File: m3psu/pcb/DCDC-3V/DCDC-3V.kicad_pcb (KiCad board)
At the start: 2 copper layers, 39.5 x 39.5 mm, 69 parts, among them IC1 LTC2975, IC2 TPS62132, IC3 LTC2975, J1 WEST TOP, J2 WEST BOT, J3 NORTH TOP, J4 EAST TOP, J5 EAST BOT, J6 NORTH BOT, Q1 NFET_GDS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

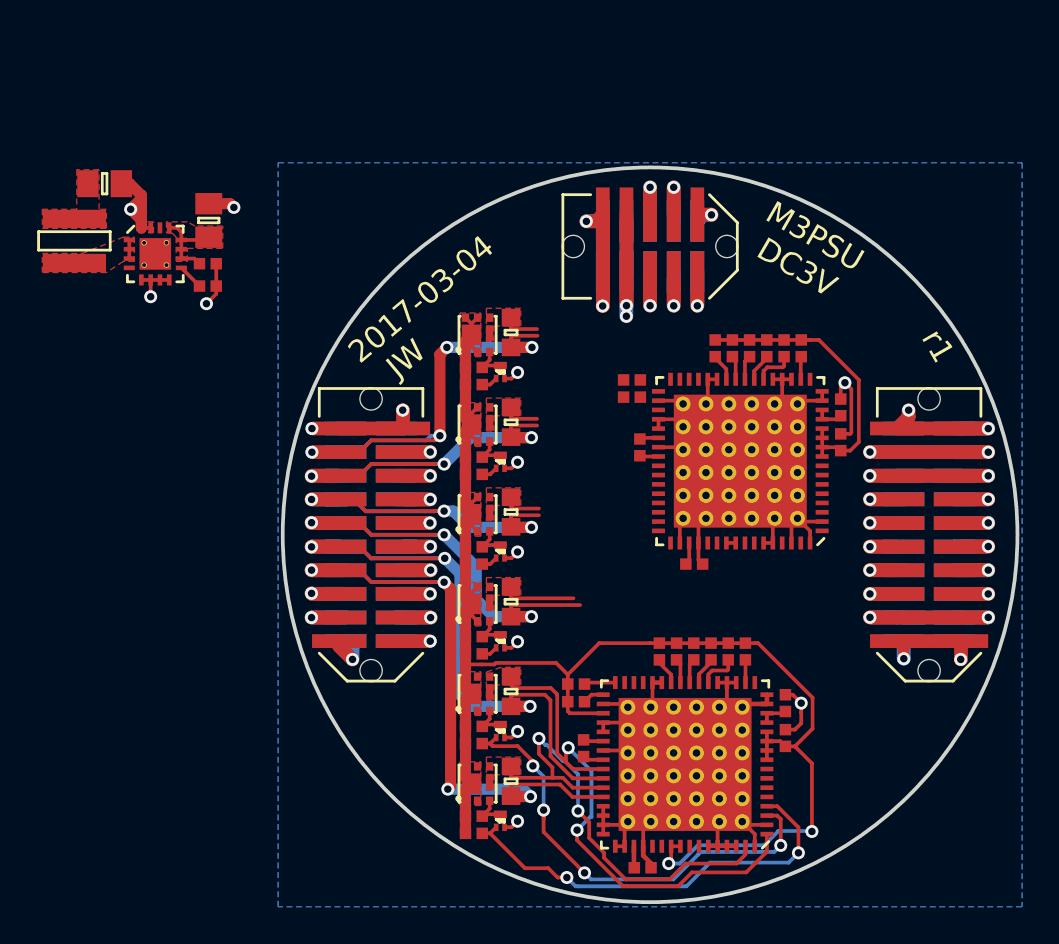
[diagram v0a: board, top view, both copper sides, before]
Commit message: Further work on routing DCDC-3V
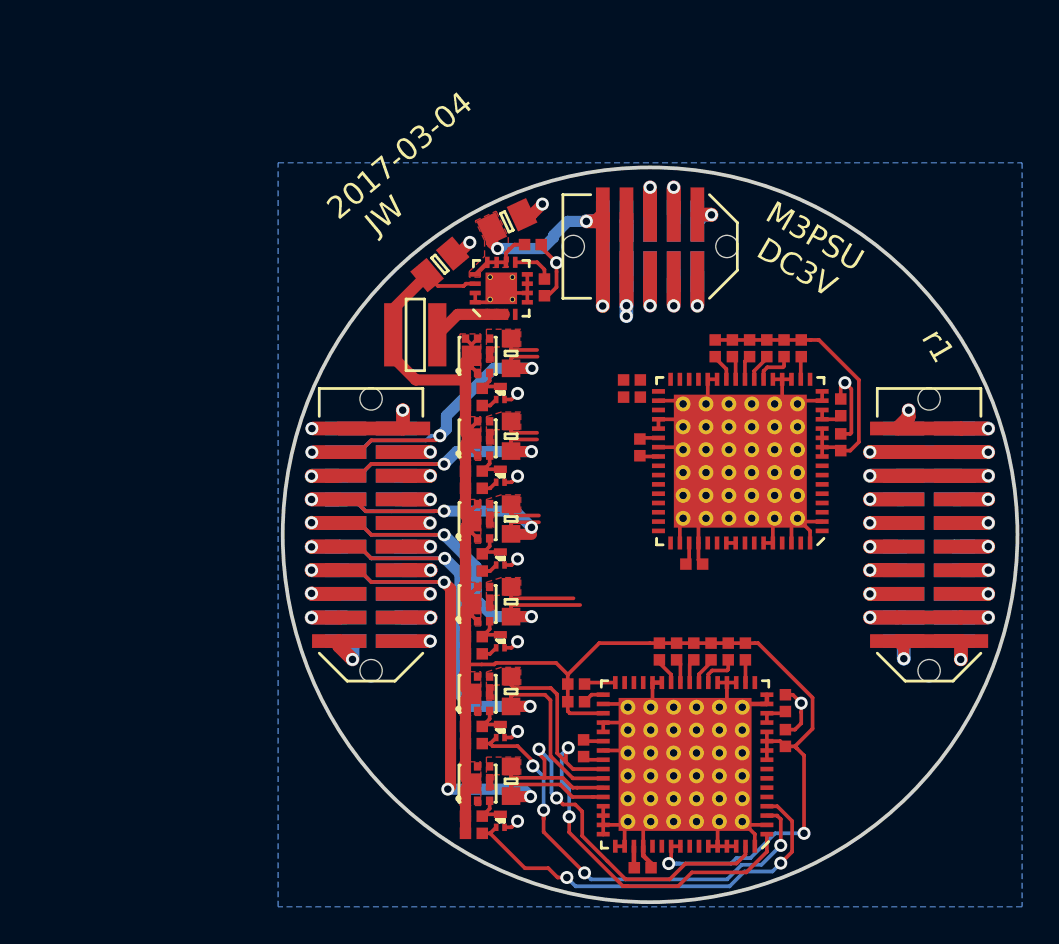
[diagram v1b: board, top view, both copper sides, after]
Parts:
- moved L1 19.0 mm to (87.4, 89.2), turned to 180 degrees
- moved IC2 18.7 mm to (92.0, 86.7), turned to 90 degrees
- moved C8 18.5 mm to (88.7, 85.5), turned to 40 degrees
- moved C7 18.1 mm to (94.3, 86.7), turned to 270 degrees
- moved C6 17.5 mm to (93.7, 84.4)
- moved C5 16.0 mm to (92.3, 83.2), turned to 25 degrees
- moved Q1 1.12 mm to (92.0, 92.4)
- moved Q5 1.12 mm to (90.7, 90.4)
- moved R13 1.12 mm to (90.5, 92.1)
- moved R17 1.12 mm to (92.5, 90.2)
- moved R9 1.12 mm to (90.5, 93.0)
- moved Q2 0.75 mm to (92.0, 96.8)
- moved Q6 0.75 mm to (90.7, 94.8)
- moved R10 0.75 mm to (90.5, 97.5)
- moved R14 0.75 mm to (90.5, 96.6)
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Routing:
- net 3v3: track 102.6 -> 113.5 mm
- net VCC: track 16.4 -> 21.7 mm, vias 2 -> 3
- net Net-(IC2-Pad1): track 1.00 -> 4.06 mm
- net /3v3_IMU: track 27.1 -> 24.5 mm, vias 4 -> 3
- net GND: track 103.4 -> 101.5 mm, vias 22 -> 21
- net /ISNS5+: track 25.2 -> 24.2 mm
- net Net-(C7-Pad1): track 1.38 -> 2.24 mm
- net /VEN_5: track 22.9 -> 22.4 mm
- removed copper zone on F.Cu, net GND
- removed copper zone on F.Cu, net Net-(IC2-Pad1)

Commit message: Finish routing DCDC-3V
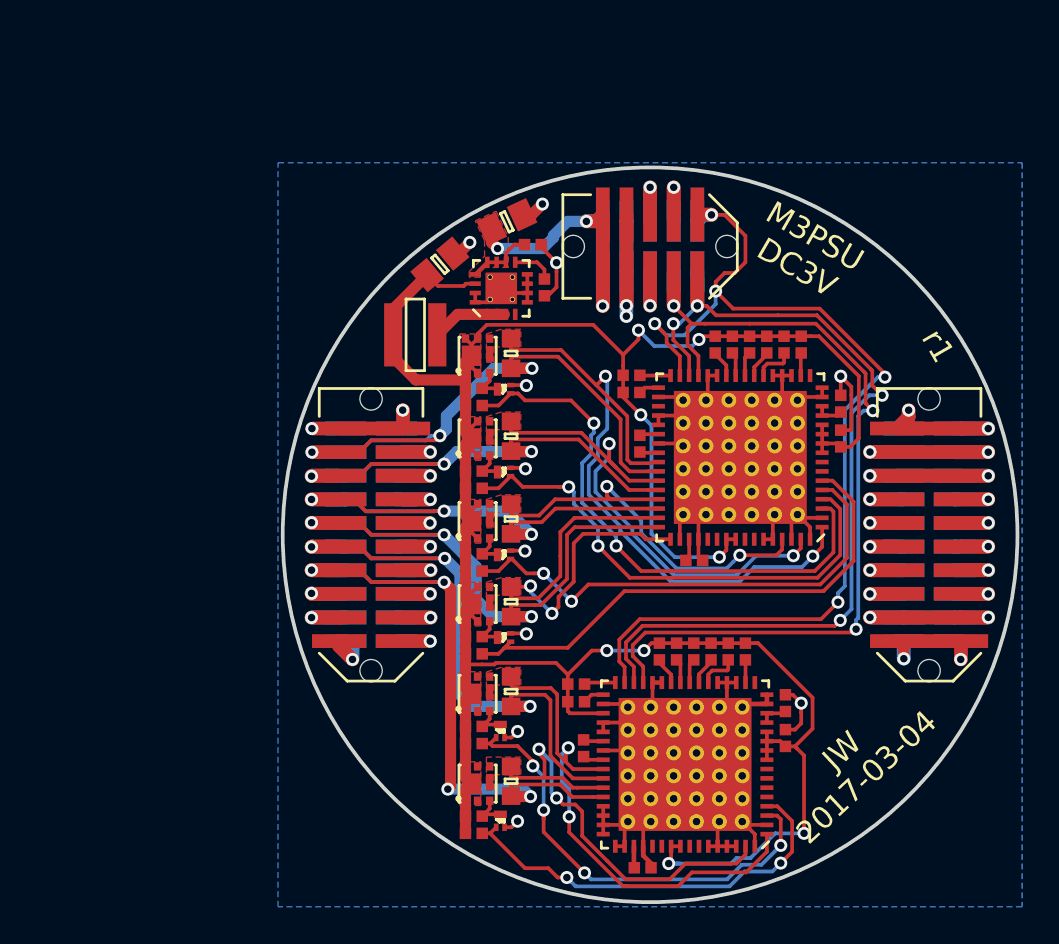
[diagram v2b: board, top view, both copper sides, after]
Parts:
- removed G***: LOGO, m3psu:cusf_logo_full
- moved Q1 0.28 mm to (92.2, 92.2), turned to 90 degrees
- moved Q2 0.28 mm to (92.2, 96.6), turned to 90 degrees
- moved Q3 0.28 mm to (92.2, 101.1), turned to 90 degrees
- moved Q4 0.28 mm to (92.2, 105.5), turned to 90 degrees
- moved R22 0.25 mm to (99.0, 92.3)
- moved R24 0.25 mm to (99.0, 91.4)
- moved C10 0.20 mm to (102.4, 101.4)
- moved C11 0.20 mm to (110.2, 93.0)
- moved C12 0.20 mm to (99.5, 95.1)
- moved C9 0.20 mm to (110.2, 94.8)
- moved IC3 0.20 mm to (104.8, 95.8)
- moved R21 0.20 mm to (104.4, 89.8)
- moved R23 0.20 mm to (106.3, 89.8)
- moved R25 0.20 mm to (107.2, 89.8)
- moved R26 0.20 mm to (108.1, 89.8)
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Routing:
- net /~ALERT: track 2.40 -> 58.3 mm, vias 1 -> 5
- net /SCL: track 3.30 -> 48.3 mm, vias 1 -> 4
- net /SDA: track 3.30 -> 47.4 mm, vias 1 -> 3
- net /ISNS0+: track 2.01 -> 36.4 mm, vias 0 -> 2
- net 3v3: track 113.5 -> 144.4 mm, vias 2 -> 8
- net /VEN_0: track 0.88 -> 30.1 mm, vias 0 -> 2
- net /VEN_3: track 0.88 -> 27.8 mm
- net /ISNS1+: track 2.10 -> 28.2 mm, vias 0 -> 2
- net /VEN_1: track 0.88 -> 26.9 mm, vias 0 -> 2
- net /VEN_2: track 0.88 -> 26.3 mm, vias 0 -> 2
- net /ISNS3+: track 3.96 -> 24.5 mm, vias 0 -> 2
- net /ISNS2+: track 2.05 -> 22.4 mm, vias 0 -> 2
- net /3v3_IMU: track 24.5 -> 34.9 mm
- net /3v3_RADIO: track 22.9 -> 30.5 mm
- net /3v3_PYRO: track 28.0 -> 35.3 mm
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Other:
- board text added: "JW 2017-03-04"
- board text removed: "2017-03-04 JW"

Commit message: Minor routing optimisation
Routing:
- net /VEN_1: track 26.9 -> 27.5 mm
- net /VEN_0: track 30.1 -> 30.7 mm

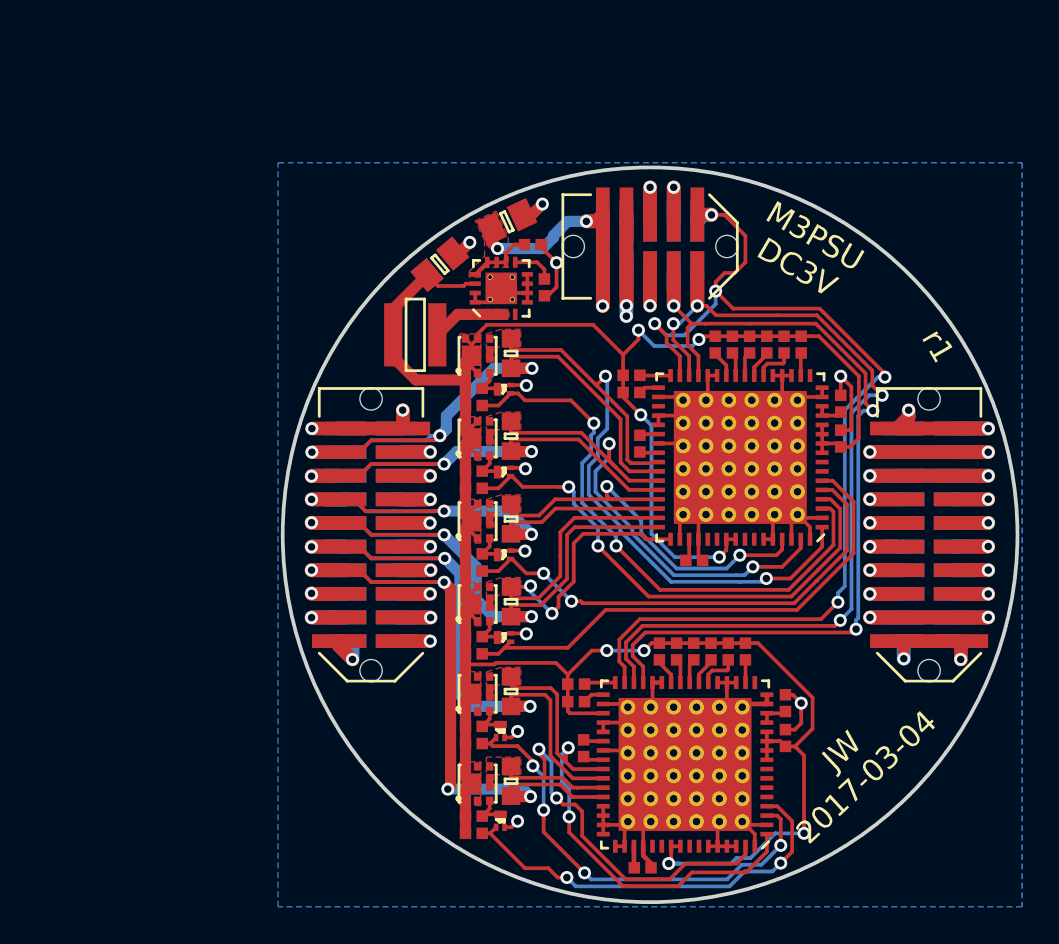
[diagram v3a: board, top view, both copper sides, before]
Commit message: Update NFET footprint, add VEN pull-downs
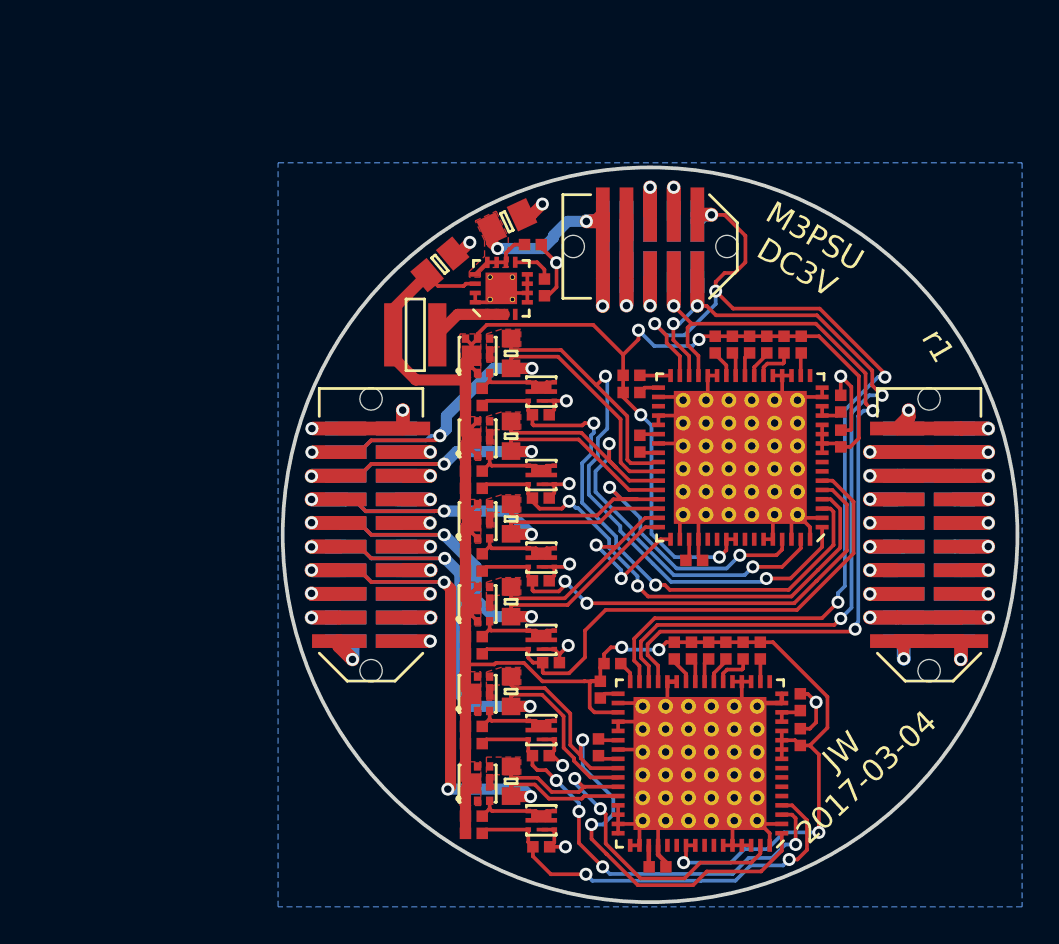
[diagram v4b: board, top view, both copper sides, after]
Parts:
- added R35: 1M, agg:0402, F.Cu at (94.1, 93.5)
- added R36: 1M, agg:0402, F.Cu at (94.1, 98.0)
- added R37: 1M, agg:0402, F.Cu at (94.1, 102.5)
- added R38: 1M, agg:0402, F.Cu at (94.7, 106.9)
- added R39: 1M, agg:0402, F.Cu at (94.1, 111.9)
- added R40: 1M, agg:0402, F.Cu at (94.2, 116.8)
- C5: value 10µ -> 10u
- C8: value 22µ -> 22u
- L1: value 2µ2 -> 2u2
- Q1, Q11, Q2, Q3, Q4, Q9: footprint agg:SOT-883-B -> agg:PowerPAK-SC-75-6L-Single
- moved R5 2.24 mm to (98.0, 106.9)
- moved Q9 2.20 mm to (94.2, 110.5), turned to 270 degrees
- moved Q11 2.20 mm to (94.2, 115.3), turned to 270 degrees
- moved Q2 2.01 mm to (94.2, 96.8), turned to 270 degrees
- moved Q3 2.01 mm to (94.2, 101.2), turned to 270 degrees
- moved Q1 2.00 mm to (94.2, 92.3), turned to 270 degrees
- moved Q4 2.00 mm to (94.2, 105.7), turned to 270 degrees
- moved R3 1.45 mm to (97.3, 108.3), turned to 270 degrees
- moved C2 0.80 mm to (100.4, 117.8)
- moved R7 0.80 mm to (103.2, 106.2)
- moved IC1 0.80 mm to (102.7, 112.3)
- moved R1 0.80 mm to (105.9, 106.2)
- moved R2 0.80 mm to (102.2, 106.2)
- moved R4 0.80 mm to (104.1, 106.2)
- moved R6 0.80 mm to (105.0, 106.2)
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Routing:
- net GND: track 101.8 -> 110.9 mm
- net /ISNS3+: track 24.5 -> 17.3 mm
- net Net-(Q2-PadD): track 1.98 -> 6.47 mm
- net Net-(Q3-PadD): track 1.98 -> 6.47 mm
- net Net-(Q1-PadD): track 1.98 -> 6.45 mm
- net Net-(Q4-PadD): track 1.98 -> 6.45 mm
- net Net-(Q11-PadD): track 2.01 -> 6.48 mm
- net Net-(Q10-PadG): track 2.01 -> 6.47 mm
- net /~ALERT: track 58.3 -> 55.6 mm
- net /ISNS5+: track 24.2 -> 21.8 mm
- net /VEN_3: track 27.6 -> 29.6 mm
- net 3v3: track 144.4 -> 145.8 mm
- net /3v3_PYRO: track 35.3 -> 33.9 mm
- net /ISNS4+: track 28.6 -> 29.8 mm
- net /VEN_5: track 22.4 -> 23.3 mm
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
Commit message: Add test pads, decoupling capacitor to 3V board
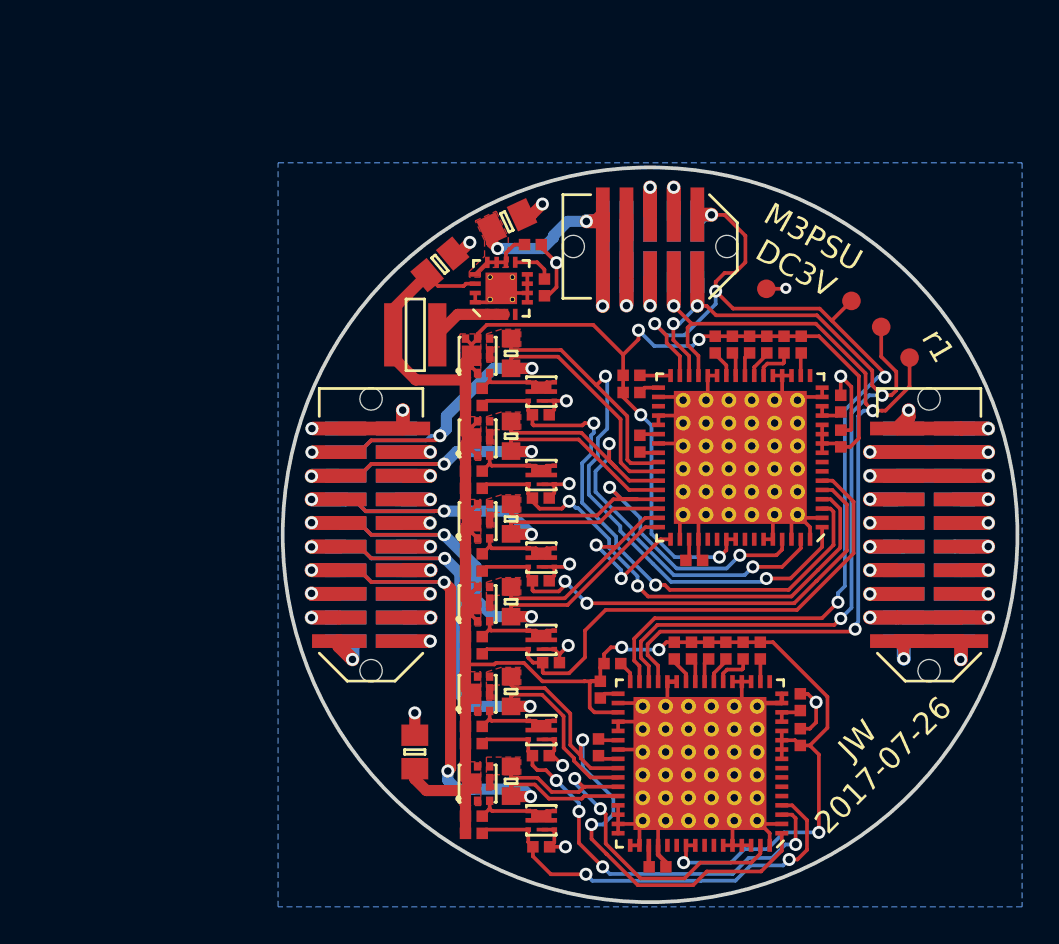
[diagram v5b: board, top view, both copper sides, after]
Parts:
- added C13: 22u, agg:0805, F.Cu at (87.3, 111.7)
- added TP1: TESTPAD, agg:TESTPAD, F.Cu at (114.0, 90.5)
- added TP2: TESTPAD, agg:TESTPAD, F.Cu at (112.4, 88.8)
- added TP3: TESTPAD, agg:TESTPAD, F.Cu at (110.8, 87.4)
- added TP4: TESTPAD, agg:TESTPAD, F.Cu at (106.2, 86.8)
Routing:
- net /SCL: track 47.4 -> 52.1 mm
- net /SDA: track 46.6 -> 50.6 mm
- net 3v3: track 145.8 -> 149.8 mm
- net GND: track 110.9 -> 113.2 mm, vias 21 -> 23
- net /~ALERT: track 55.6 -> 57.1 mm
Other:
- board text added: "JW 2017-07-26"
- board text removed: "JW 2017-03-04"

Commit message: Add logo to 3V board
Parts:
- added G***: LOGO, m3psu:cusf_logo_full, B.Cu at (99.8, 100.4)
